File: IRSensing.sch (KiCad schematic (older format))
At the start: 0 parts

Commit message: Added IR Sensor foorprint + PCB
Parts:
- added U?: OPB733TR, symbol OPB733TR
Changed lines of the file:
@@
 LIBS:contrib
 LIBS:valves
+LIBS:smallGroundRobot-cache
 EELAYER 25 0
 EELAYER END
 $Descr A4 11693 8268
 encoding utf-8
-Sheet 1 7
+Sheet 5 8
 Title ""
 Date ""
@@
 Comment4 ""
 $EndDescr
+$Comp
+L OPB733TR U?
+U 1 1 5A9B4417
+P 5450 3100
+F 0 "U?" H 5450 2800 60  0000 C CNN
+F 1 "OPB733TR" H 5450 3400 60  0000 C CNN
+F 2 "" H 5350 2700 60  0001 C CNN
+F 3 "http://www.ttelectronics.com/sites/default/files/download-files/OPB733TR.pdf" H 5450 2700 60  0001 C CNN
+	1    5450 3100
+	1    0    0    -1
+$EndComp
 $EndSCHEMATC

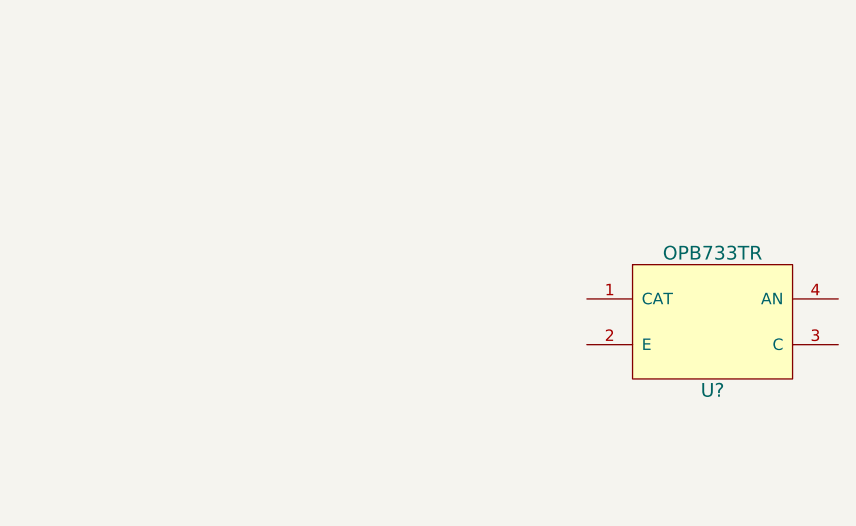
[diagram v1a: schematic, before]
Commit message: Adding IR sensor circuit
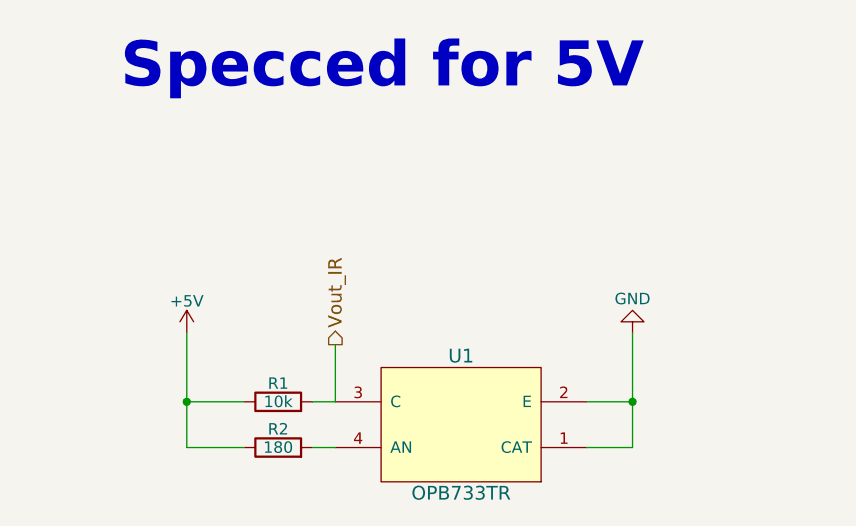
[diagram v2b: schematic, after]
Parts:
- added R1: 10k, Resistors_SMD:R_0805, symbol R
- added R2: 180, Resistors_SMD:R_0805, symbol R
- U1: renamed from U?; footprint (none) -> Custom:OPB733TR
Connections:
- net GND: now reaches U1.1 (CAT)
- net GND: now also U1.2 (E)
- net Vout_IR: now reaches U1.3 (C)
- net Vout_IR: now also R1.2
- net at U1.4 (AN): now also R2.2
- new net +5V: R1.1, R2.1
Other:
- note added: "Specced for 5V"
- moved on the sheet: U1
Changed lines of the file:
@@
 $EndDescr
 $Comp
-L OPB733TR U?
+L OPB733TR U1
 U 1 1 5A9B4417
-P 5450 3100
-F 0 "U?" H 5450 2800 60  0000 C CNN
-F 1 "OPB733TR" H 5450 3400 60  0000 C CNN
-F 2 "" H 5350 2700 60  0001 C CNN
-F 3 "http://www.ttelectronics.com/sites/default/files/download-files/OPB733TR.pdf" H 5450 2700 60  0001 C CNN
-	1    5450 3100
+P 4350 3550
+F 0 "U1" H 4350 3250 60  0000 C CNN
+F 1 "OPB733TR" H 4350 3850 60  0000 C CNN
+F 2 "Custom:OPB733TR" H 4250 3150 60  0001 C CNN
+F 3 "http://www.ttelectronics.com/sites/default/files/download-files/OPB733TR.pdf" H 4350 3150 60  0001 C CNN
+	1    4350 3550
+	-1   0    0    1
+$EndComp
+Text Notes 5150 2100 2    197  ~ 39
+Specced for 5V
+$Comp
+L R R2
+U 1 1 5A9DC177
+P 3550 3650
+F 0 "R2" V 3630 3650 50  0000 C CNN
+F 1 "180" V 3550 3650 50  0000 C CNN
+F 2 "Resistors_SMD:R_0805" V 3480 3650 50  0001 C CNN
+F 3 "" H 3550 3650 50  0001 C CNN
+	1    3550 3650
+	0    -1   -1   0
+$EndComp
+$Comp
+L R R1
+U 1 1 5A9DC2E1
+P 3550 3450
+F 0 "R1" V 3630 3450 50  0000 C CNN
+F 1 "10k" V 3550 3450 50  0000 C CNN
+F 2 "Resistors_SMD:R_0805" V 3480 3450 50  0001 C CNN
+F 3 "" H 3550 3450 50  0001 C CNN
+	1    3550 3450
+	0    -1   -1   0
+$EndComp
+$Comp
+L GND #PWR01
+U 1 1 5A9DC3A0
+P 5100 3150
+F 0 "#PWR01" H 5100 2900 50  0001 C CNN
+F 1 "GND" H 5100 3000 50  0000 C CNN
+F 2 "" H 5100 3150 50  0001 C CNN
+F 3 "" H 5100 3150 50  0001 C CNN
+	1    5100 3150
+	-1   0    0    1
+$EndComp
+Wire Wire Line
+	4900 3450 5100 3450
+Wire Wire Line
+	4900 3650 5100 3650
+Connection ~ 5100 3450
+Wire Wire Line
+	3400 3450 3150 3450
+Wire Wire Line
+	3150 3650 3150 3150
+Wire Wire Line
+	3400 3650 3150 3650
+Connection ~ 3150 3450
+Wire Wire Line
+	3700 3650 3800 3650
+Wire Wire Line
+	3700 3450 3800 3450
+$Comp
+L +5V #PWR02
+U 1 1 5A9DC59B
+P 3150 3150
+F 0 "#PWR02" H 3150 3000 50  0001 C CNN
+F 1 "+5V" H 3150 3290 50  0000 C CNN
+F 2 "" H 3150 3150 50  0001 C CNN
+F 3 "" H 3150 3150 50  0001 C CNN
+	1    3150 3150
 	1    0    0    -1
 $EndComp
+Wire Wire Line
+	5100 3650 5100 3150
+Wire Wire Line
+	3800 3450 3800 3200
+Text HLabel 3800 3200 1    59   Output ~ 0
+Vout_IR
 $EndSCHEMATC
